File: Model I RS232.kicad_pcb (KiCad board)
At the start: 2 copper layers, 115 x 74 mm, 28 parts, among them U1 HD6402, U10 74LS08, U2 COM8116, U3 74LS155, U4 74LS04, U5 74LS00, U6 74LS244, U7 74LS367, U8 74LS174, U9 SP3243ECA-L/TR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

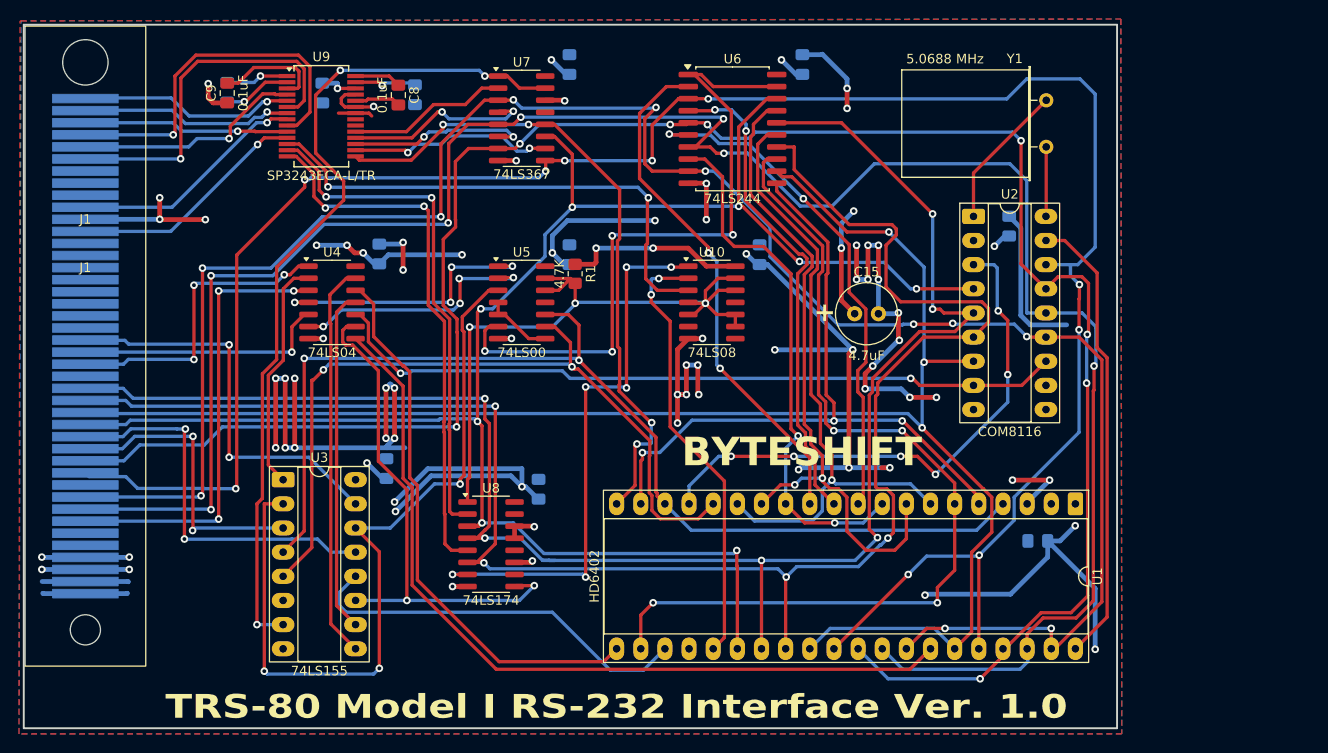
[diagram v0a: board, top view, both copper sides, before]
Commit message: Add files via upload
trimmed PCB size a bit to clear support post
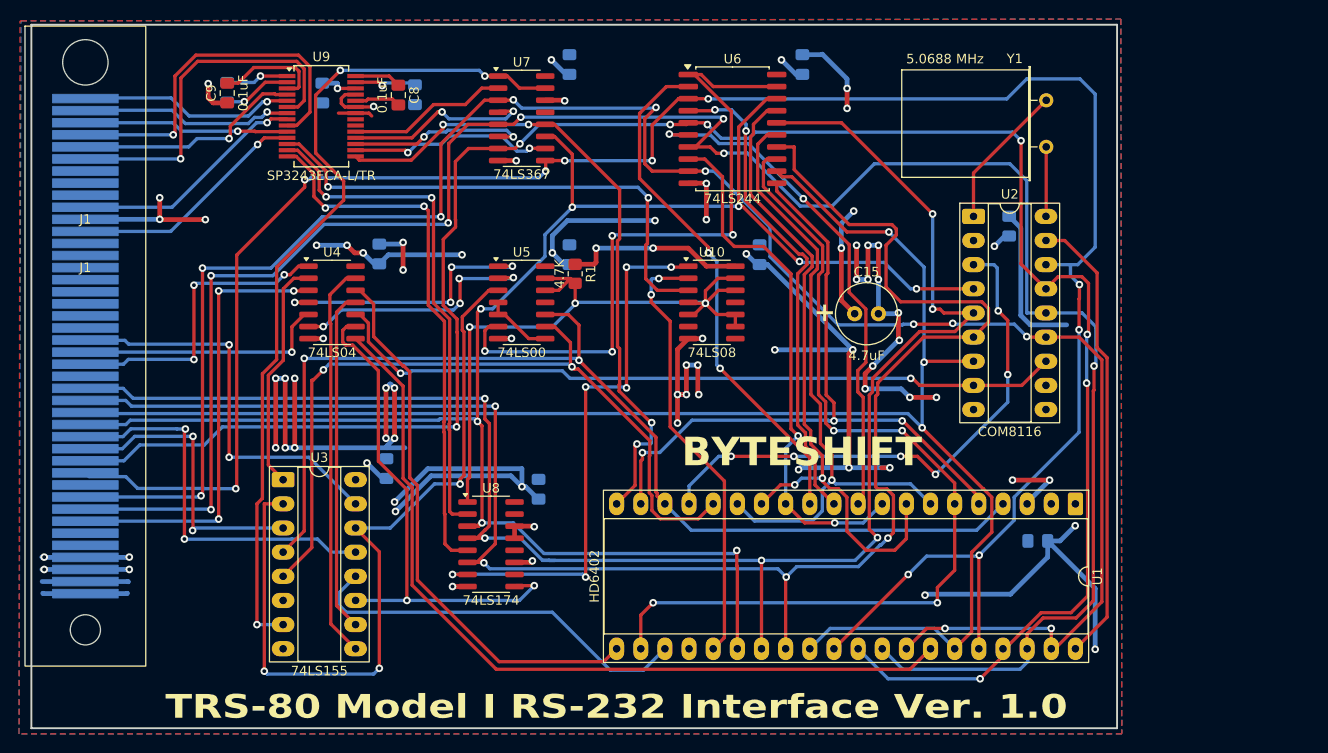
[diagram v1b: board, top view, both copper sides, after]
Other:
- board size 115 x 74 mm -> 114.2 x 74 mm

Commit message: Add files via upload
Update schematic and PCB to version 1.1 -- 05 April 2025

1. change PCB footprint to eliminate mechanical interference with mounting post
2. modify footprint of J1 pads to fit more closely
3. fix schematic error causing U9 to be in permanent shutdown mode
4. Clean up some very ugly routing
5. Change version information on silkscreen
6. embed silkscreen logo as footprint to fix missing font error
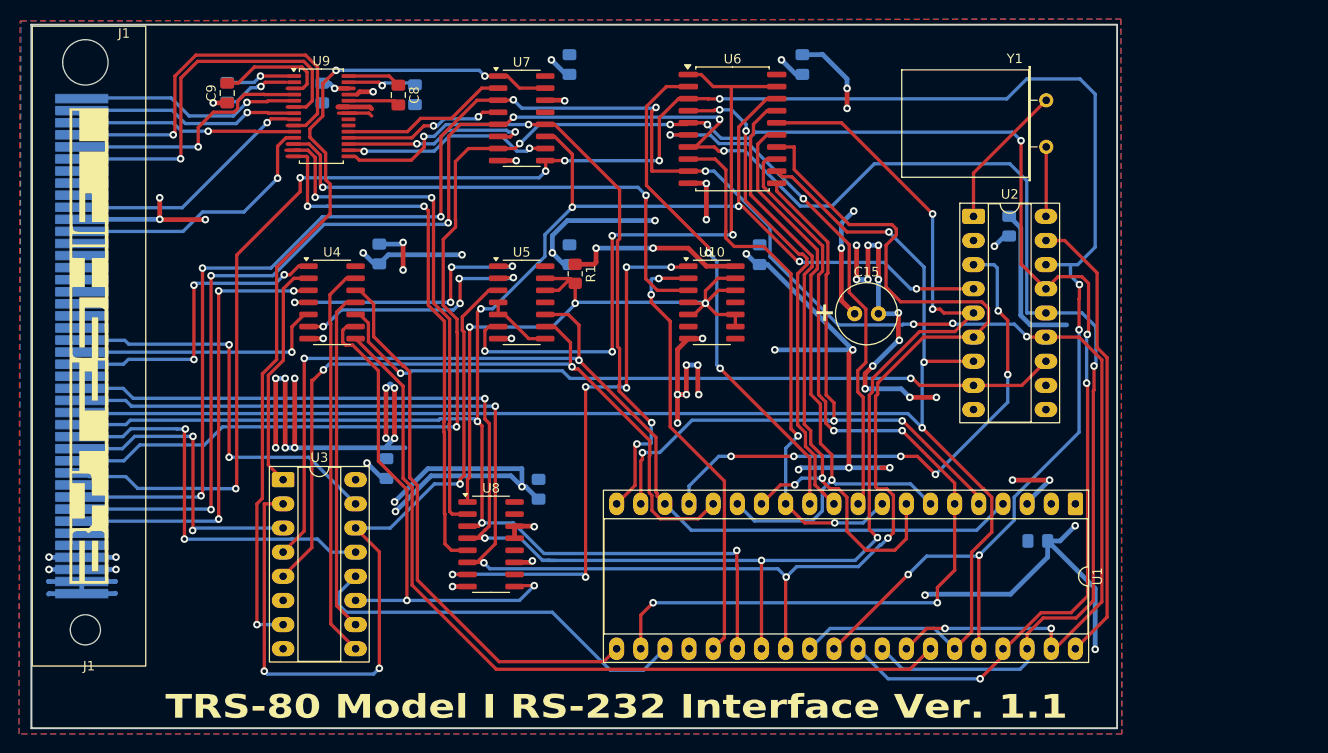
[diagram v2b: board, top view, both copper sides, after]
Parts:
- added G***: LOGO, LOGO, F.Cu at (82.0, 108.4)
- C1, C10, C11, C12, C13, C14, C2, C3, C4, C5, C6, C7, C8, C9: footprint ModelIRS232:C_0805_2012Metric_Pad1.18x1.45mm_HandSolder -> Capacitor_SMD:C_0805_2012Metric_Pad1.18x1.45mm_HandSolder
- C15: footprint ModelIRS232:C_Radial_D6.3mm_H11.0mm_P2.50mm -> Capacitor_THT:C_Radial_D6.3mm_H11.0mm_P2.50mm
- J1: footprint ModelIRS232:TRS-80 M1 EI_ADDON_42P_CONN -> Byteshift_Library:TRS-80 M1 EI_ADDON_42P_CONN
- R1: footprint ModelIRS232:R_0805_2012Metric_Pad1.20x1.40mm_HandSolder -> Resistor_SMD:R_0805_2012Metric_Pad1.20x1.40mm_HandSolder
- U1: footprint ModelIRS232:DIP-40_W15.24mm_Socket_LongPads -> Package_DIP:DIP-40_W15.24mm_Socket_LongPads
- U10, U4, U5: footprint ModelIRS232:SOIC-14_3.9x8.7mm_P1.27mm -> Package_SO:SOIC-14_3.9x8.7mm_P1.27mm
- U2: footprint ModelIRS232:DIP-18_W7.62mm_Socket_LongPads -> Package_DIP:DIP-18_W7.62mm_Socket_LongPads
- U3: footprint ModelIRS232:DIP-16_W7.62mm_Socket_LongPads -> Package_DIP:DIP-16_W7.62mm_Socket_LongPads
- U6: footprint ModelIRS232:SOIC-20W_7.5x12.8mm_P1.27mm -> Package_SO:SOIC-20W_7.5x12.8mm_P1.27mm
- U7, U8: footprint ModelIRS232:SOIC-16_3.9x9.9mm_P1.27mm -> Package_SO:SOIC-16_3.9x9.9mm_P1.27mm
- U9: footprint ModelIRS232:SSOP-28_5.3x10.2mm_P0.65mm -> Package_SO:TSSOP-28_4.4x9.7mm_P0.65mm
- Y1: footprint ModelIRS232:Crystal_HC49-U_Horizontal -> Crystal:Crystal_HC49-U_Horizontal
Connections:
- U9 pad 23: GND -> VCC
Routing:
- net GND: track 204.1 -> 195.4 mm
- net VCC: track 210.7 -> 205.2 mm, vias 31 -> 29
- net Net-(U7-I2): track 19.9 -> 16.3 mm
- net Net-(U6A-~{OE}): track 71.1 -> 68.3 mm
- net TXD: track 25.3 -> 27.3 mm
- net DTR: track 38.9 -> 40.5 mm
- net CD: track 38.0 -> 39.6 mm
- net Net-(U9-V-): track 11.4 -> 12.9 mm
- net Net-(U8-Q1): track 57.2 -> 58.7 mm
- net CTS: track 24.2 -> 25.2 mm
- net Net-(U9-T3IN): track 54.8 -> 55.6 mm
- net Net-(U8-Q0): track 54.2 -> 55.0 mm
- net Net-(U1-PARERR): track 56.2 -> 56.9 mm
- net Net-(U1-RXBUF0): track 54.8 -> 54.2 mm
- net Net-(U1-RX_SERIAL): track 69.7 -> 70.2 mm
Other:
- board text added: "TRS-80 Model I RS-232 Interface Ver. 1.1"
- board text removed: "BYTESHIFT"
- board text removed: "TRS-80 Model I RS-232 Interface Ver. 1.0"

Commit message: Add files via upload
Updated local footprint for J1
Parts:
- J1: footprint Byteshift_Library:TRS-80 M1 EI_ADDON_42P_CONN -> ModelIRS232:TRS-80 M1 EI_ADDON_42P_CONN

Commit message: Add files via upload
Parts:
- added J2: Conn_01x03_Pin, Connector_PinHeader_2.54mm:PinHeader_1x03_P2.54mm_Vertical, F.Cu at (142.8, 77.8)
- added J3: Conn_01x04_Pin, Connector_PinHeader_2.54mm:PinHeader_1x04_P2.54mm_Vertical, F.Cu at (167.1, 77.9)
- added J4: Conn_01x02_Pin, Connector_PinHeader_2.54mm:PinHeader_1x02_P2.54mm_Vertical, F.Cu at (155.8, 77.8)
- added J5: Conn_01x02_Pin, Connector_PinHeader_2.54mm:PinHeader_1x02_P2.54mm_Vertical, F.Cu at (93.1, 90.8)
- C11: value 0.47uF -> 0.1uF
- C15: footprint Capacitor_THT:C_Radial_D6.3mm_H11.0mm_P2.50mm -> Capacitor_SMD:C_0805_2012Metric_Pad1.18x1.45mm_HandSolder; moved to B.Cu
- C8, C9: moved to B.Cu
- J1: footprint ModelIRS232:TRS-80 M1 EI_ADDON_42P_CONN -> Byteshift_Library:TRS-80 M1 EI_ADDON_42P_CONN
- U3: footprint Package_DIP:DIP-16_W7.62mm_Socket_LongPads -> Package_SO:SOIC-16_3.9x9.9mm_P1.27mm
- U9: footprint Package_SO:TSSOP-28_4.4x9.7mm_P0.65mm -> Package_SO:SSOP-28_5.3x10.2mm_P0.65mm
- moved C15 77.6 mm to (90.7, 134.4), turned to 90 degrees
- moved Y1 49.5 mm to (142.0, 110.8), turned to 180 degrees
- moved U6 49.4 mm to (120.0, 125.0)
- moved C6 48.9 mm to (128.1, 118.2)
- moved C1 47.7 mm to (157.1, 88.1), turned to 0 degrees
- moved U1 47.5 mm to (153.2, 90.4), turned to 0 degrees
- moved C5 46.7 mm to (139.3, 120.9), turned to 0 degrees
- moved U2 45.7 mm to (135.9, 118.3)
- moved C12 41.7 mm to (107.0, 131.8), turned to 0 degrees
- moved U5 41.6 mm to (100.9, 135.8)
- moved U8 25.3 mm to (119.9, 104.3)
- moved C14 24.3 mm to (138.6, 78.8), turned to 0 degrees
- moved C7 23.8 mm to (125.9, 99.8), turned to 0 degrees
- moved U10 21.9 mm to (135.1, 85.8)
- moved R1 15.9 mm to (127.9, 85.8), turned to 0 degrees
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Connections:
- net Net-(U1-RX_SERIAL) renamed RX_TTL
- net Net-(U9-T3IN) renamed TX_TTL
- U9 pad 22: VCC -> ~{SHUTDOWN}
- Y1 pad 1: Net-(U2-XTAL/EXT1) -> Net-(U2-XTAL/EXT2)
- Y1 pad 2: Net-(U2-XTAL/EXT2) -> Net-(U2-XTAL/EXT1)
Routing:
- net GND: track 195.4 -> 107.9 mm, vias 49 -> 15
- net VCC: track 205.2 -> 125.2 mm, vias 29 -> 22
- net D4: track 230.5 -> 159.4 mm, vias 10 -> 5
- net RX_TTL: track 70.2 -> 134.9 mm, vias 4 -> 2
- net D6: track 227.8 -> 174.6 mm, vias 7 -> 5
- net Net-(U3-Ea2): track 83.5 -> 31.6 mm, vias 3 -> 2
- net Net-(U1-~{TXLOAD}): track 41.8 -> 91.0 mm, vias 0 -> 2
- net ~{SHUTDOWN}: track 0.00 -> 46.1 mm
- net D1: track 180.2 -> 134.4 mm, vias 6 -> 3
- net Net-(U1-RESET): track 58.5 -> 103.3 mm, vias 0 -> 3
- net Net-(U1-TX_SERIAL): track 46.5 -> 85.7 mm, vias 2 -> 1
- net D0: track 190.3 -> 152.9 mm, vias 8 -> 4
- net Net-(U8-Q1): track 58.7 -> 27.6 mm
- net Net-(U8-Q0): track 55.0 -> 24.6 mm, vias 2 -> 0
- net Net-(U3-Q0a): track 89.0 -> 62.0 mm, vias 3 -> 2
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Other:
- board size 114.2 x 74 mm -> 98.5 x 72.1 mm
- board text added: "GND GND +5V"
- board text added: "LOOP BACK TEST"
- board text added: "Line Driver Normal Shutdown"
- board text added: "TRS-80 Model I RS-232 Interface Ver. 2.1"
- board text added: "TX_TTL RX_TTL"
- board text added: "made in frustration"
- board text removed: "+"
- board text removed: "TRS-80 Model I RS-232 Interface Ver. 1.1"
